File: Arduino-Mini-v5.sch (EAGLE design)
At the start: 35 parts, among them IC1 LP2985AIM5-5.0, SW1 RESET, U1 ATMEGA328P-MU, X2 16MHz

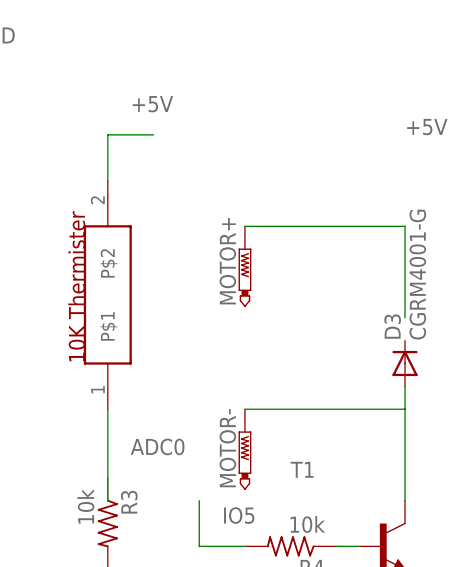
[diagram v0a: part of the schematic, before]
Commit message: placed parts, no routes
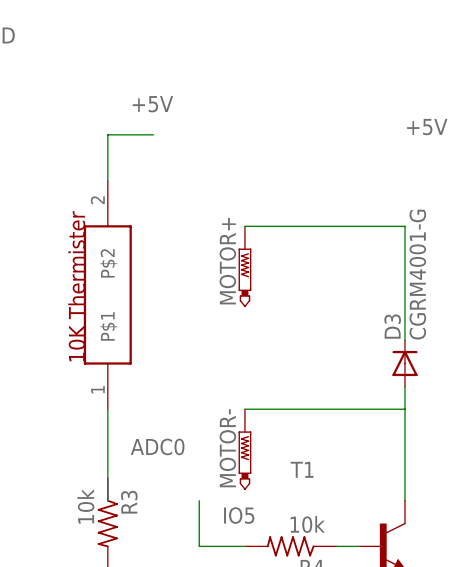
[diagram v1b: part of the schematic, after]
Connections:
- net +5V: now also D3.C
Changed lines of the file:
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@@
 </segment>
 <segment>
-<wire x1="375.92" y1="43.18" x2="375.92" y2="53.34" width="0.1524" layer="91"/>
+<wire x1="375.92" y1="40.64" x2="375.92" y2="53.34" width="0.1524" layer="91"/>
 <label x="375.92" y="63.5" size="1.778" layer="95"/>
 <wire x1="358.14" y1="53.34" x2="375.92" y2="53.34" width="0.1524" layer="91"/>
 <pinref part="MOTOR+" gate="G$1" pin="TP"/>
+<pinref part="D3" gate="G$1" pin="C"/>
 </segment>
 </net>

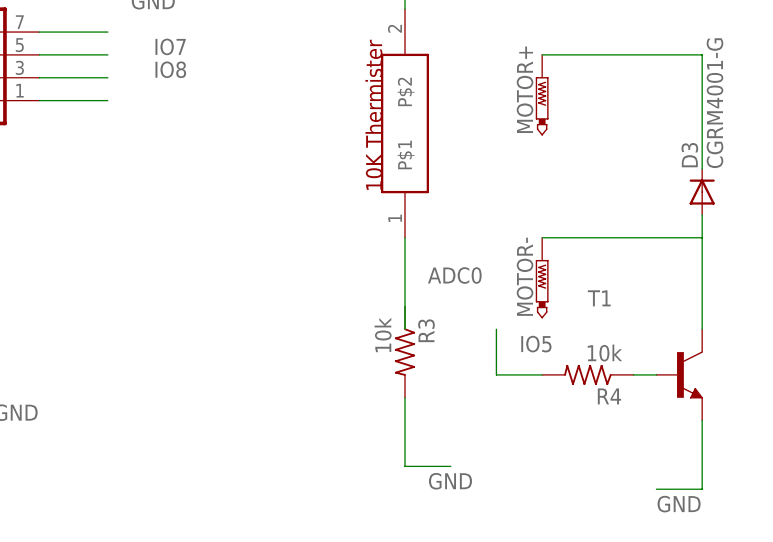
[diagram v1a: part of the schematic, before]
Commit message: fixing the thermister flaw
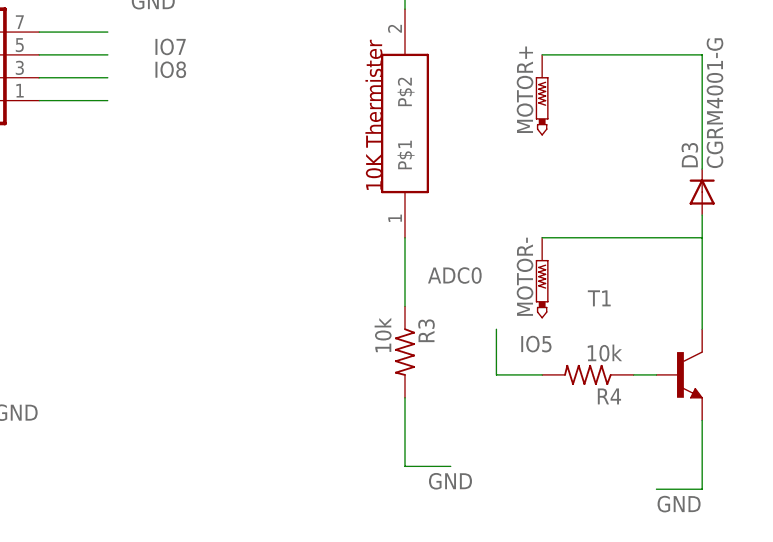
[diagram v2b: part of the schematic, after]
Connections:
- net ADC0: now also R3.1
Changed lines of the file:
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@@
 <segment>
 <pinref part="U$12" gate="G$1" pin="P$1"/>
-<wire x1="342.9" y1="33.02" x2="342.9" y2="22.86" width="0.1524" layer="91"/>
+<wire x1="342.9" y1="33.02" x2="342.9" y2="25.4" width="0.1524" layer="91"/>
 <label x="345.44" y="27.94" size="1.778" layer="95"/>
+<pinref part="R3" gate="G$1" pin="1"/>
 </segment>
 </net>
